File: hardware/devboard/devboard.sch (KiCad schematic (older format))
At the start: 19 parts

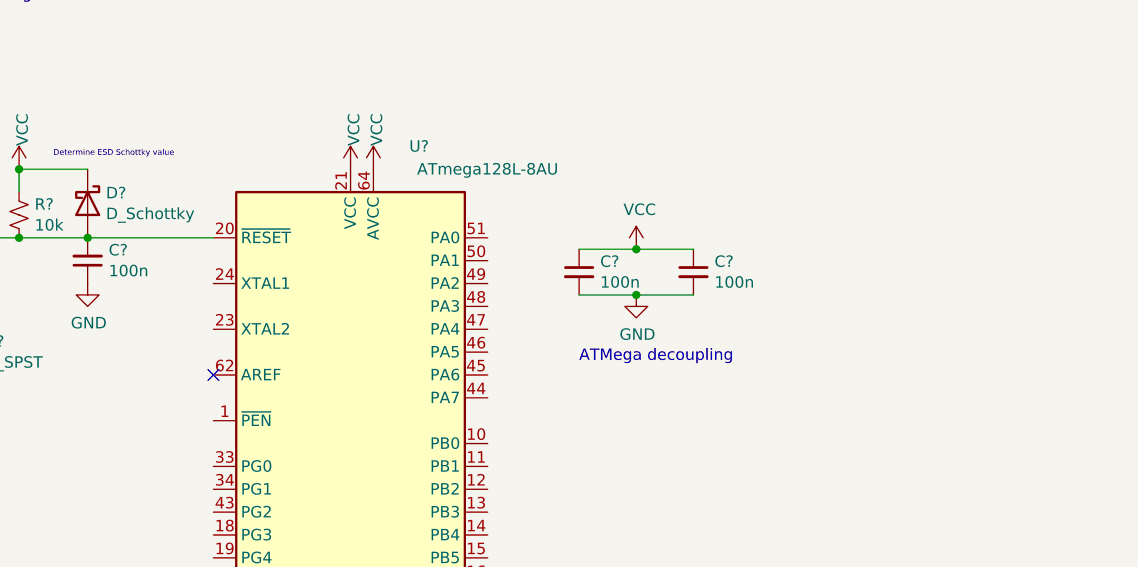
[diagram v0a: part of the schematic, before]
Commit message: Tie xtal pins to ground for now
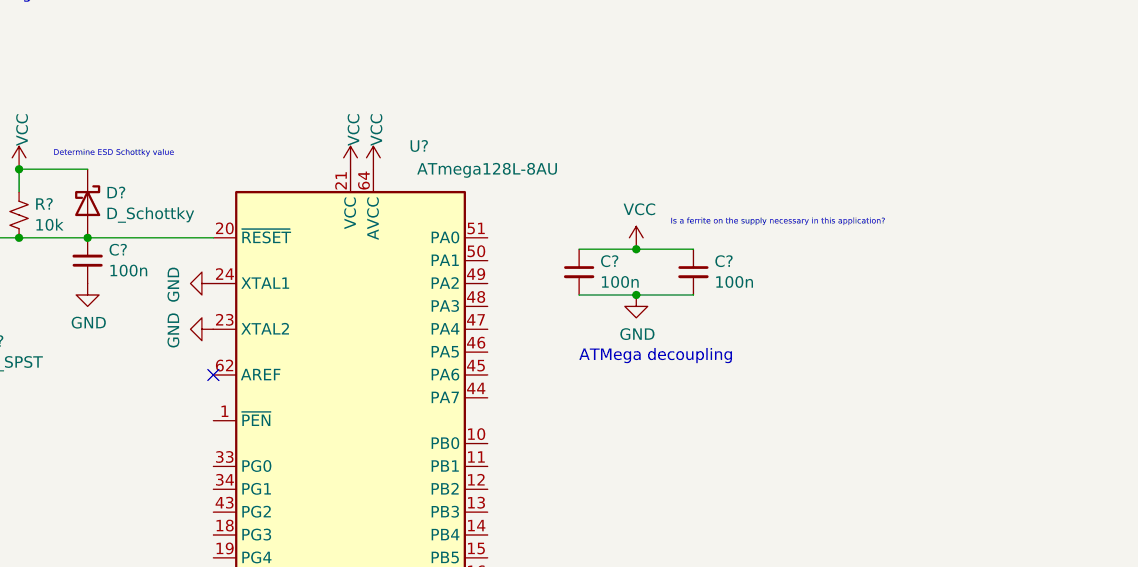
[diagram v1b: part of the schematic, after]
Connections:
- net GND: now also U?.23 (XTAL2), U?.24 (XTAL1)
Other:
- note added: "Is a ferrite on the supply necessary in this application?"
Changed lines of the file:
@@
 	1    0    0    -1
 $EndComp
+$Comp
+L power:GND #PWR?
+U 1 1 5FDE214E
+P 2050 2400
+F 0 "#PWR?" H 2050 2150 50  0001 C CNN
+F 1 "GND" H 2055 2227 50  0000 C CNN
+F 2 "" H 2050 2400 50  0001 C CNN
+F 3 "" H 2050 2400 50  0001 C CNN
+	1    2050 2400
+	0    1    1    0
+$EndComp
+$Comp
+L power:GND #PWR?
+U 1 1 5FDE278B
+P 2050 2600
+F 0 "#PWR?" H 2050 2350 50  0001 C CNN
+F 1 "GND" H 2055 2427 50  0000 C CNN
+F 2 "" H 2050 2600 50  0001 C CNN
+F 3 "" H 2050 2600 50  0001 C CNN
+	1    2050 2600
+	0    1    1    0
+$EndComp
+Text Notes 4050 2150 0    25   ~ 0
+Is a ferrite on the supply necessary in this application?
 $EndSCHEMATC

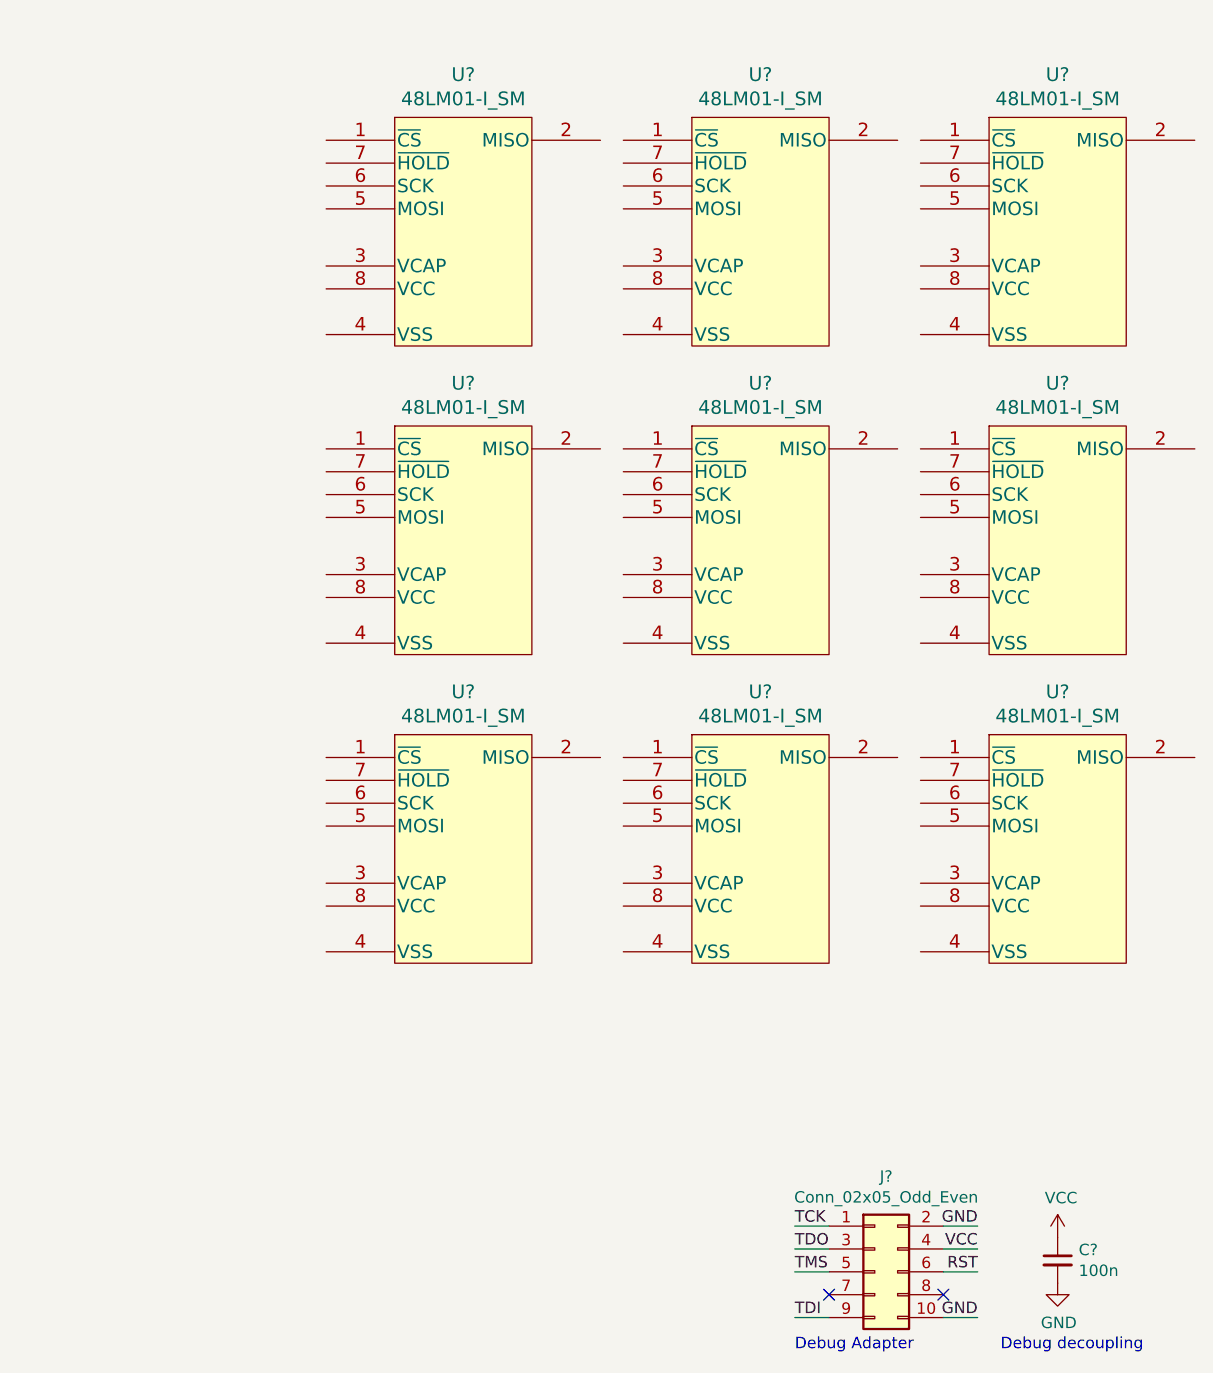
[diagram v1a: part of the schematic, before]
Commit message: Add memory banks
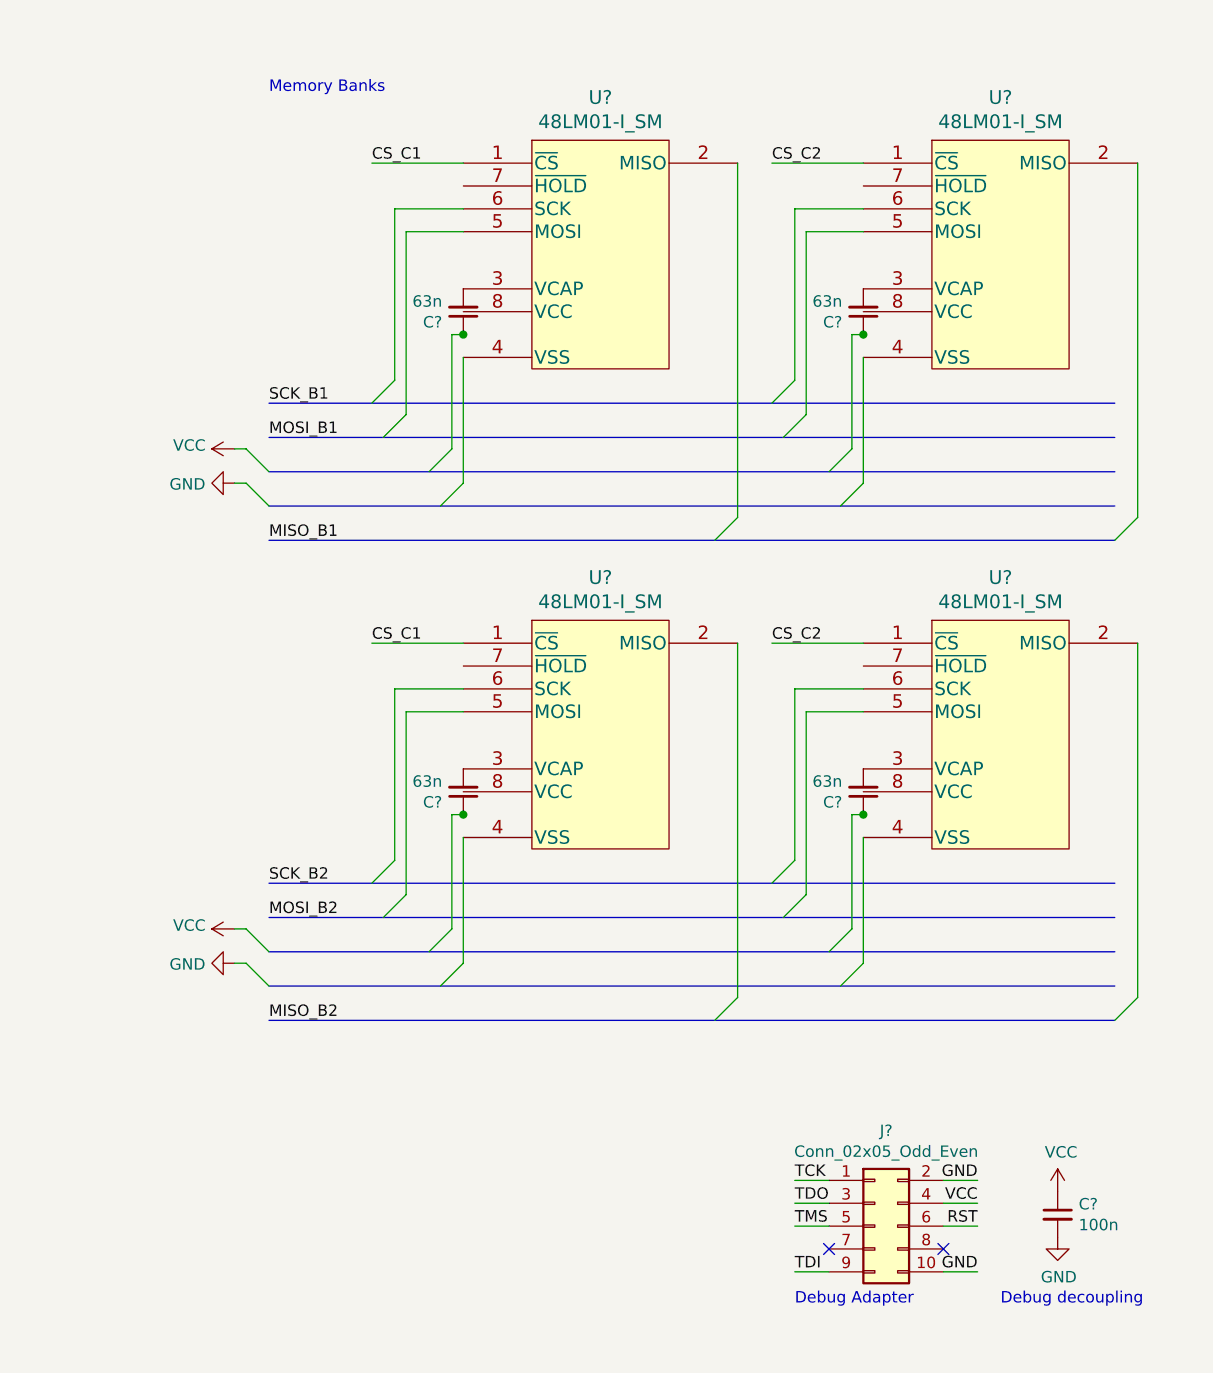
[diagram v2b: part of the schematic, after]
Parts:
- removed U? (x8): 48LM01-I_SM, SOIJ8_SM_MCH, symbol davinci:48LM01-I_SM
- added C? (x4): 63n, symbol Device:C_Small
- added U? (x3): 48LM01-I_SM, SOIJ8_SM_MCH, symbol davinci:48LM01-I_SM
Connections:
- net CS_C2: now reaches U?.1 (~CS)
- net CS_C2: now also U?.1 (~CS)
- net at U?.3 (VCAP): now also C?.2
- new net: C?.2, U?.3 (VCAP) (x3)
- new net CS_C1: U?.1 (~CS), U?.1 (~CS)
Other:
- note added: "Memory Banks"
- moved on the sheet: C?, J?, U?

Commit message: Add more memory, watchdog, buffers, test points
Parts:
- removed C? (x3): 63n, symbol Device:C_Small
- removed U? (x3): 48LM01-I_SM, SOIJ8_SM_MCH, symbol davinci:48LM01-I_SM
- added C? (x8): 63n, symbol Device:C_Small
- added C?: 100n, symbol Device:C_Small
- added R? (x3): 10k, symbol Device:R_Small_US
- added TP? (x3): TestPoint_2Pole, TestPoint:TestPoint_Bridge_Pitch2.54mm_Drill1.0mm, symbol Connector:TestPoint_2Pole
- added U? (x8): 48LM01-I_SM, SOIJ8_SM_MCH, symbol davinci:48LM01-I_SM
- added U? (x3): MC74VHCT126ADR2G, SOIC-14_NB_ONS, symbol davinci:MC74VHCT126ADR2G
- added U?: MAX6371, Package_TO_SOT_SMD:SOT-23-8, symbol Power_Supervisor:MAX6371
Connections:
- net labels added: B1_C1_HOLD, B1_C2_HOLD, B1_C3_HOLD, B1_EN, B1_MISO, B1_MOSI, B1_SCK, B2_C1_HOLD, B2_C2_HOLD, B2_C3_HOLD, B2_EN, B2_MISO, B2_MOSI, B2_SCK, B3_C1_HOLD, B3_C2_HOLD, B3_C3_HOLD, B3_EN, B3_MISO, B3_MOSI, B3_SCK, C1_CS, C2_CS, C3_CS, MISO, MOSI, SCK, WDI
- net labels removed: CS_C1, CS_C2, MISO_B1, MISO_B2, MOSI_B1, MOSI_B2, SCK_B1, SCK_B2
- wire segments 64 -> 125
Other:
- note added: "CRITICAL ELEMENTS:\nMCU\nReset circuit\nDebug circuit\nExternal tuning or clock oscillator?\nOBC connector testpads\nDedicated watchdog\nTest points"
- note added: "CRITICAL NOTES:\nCapacitors must be C0G with 60% voltage derate"
- note added: "Choose TWD, current selection is 3 seconds"
- note added: "Current limiting on set shouldn't be necessary, check this"
- note added: "Watchdog"
- note removed: "CRITICAL ELEMENTS:\nMCU\nReset circuit\nDebug circuit\nExternal tuning or clock oscillator?\nInter-element connector\nOBC connector\nDedicated watchdog\nTest points"
- note removed: "CRITICAL NOTES:\nUse Tantalum capacitors"
- note removed: "Debug decoupling"
- moved on the sheet: C?, D?, J?, R?, SW?, U?

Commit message: Add LDO for 5V supply
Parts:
- removed TP? (x3): TestPoint_2Pole, TestPoint:TestPoint_Bridge_Pitch2.54mm_Drill1.0mm, symbol Connector:TestPoint_2Pole
- added C? (x2): 1u, symbol Device:C_Small
- added TP? (x20): TestPoint, TestPoint:TestPoint_Bridge_Pitch2.54mm_Drill1.0mm, symbol Connector:TestPoint
- added U?: AP2112K-3.3, Package_TO_SOT_SMD:SOT-23-5, symbol Regulator_Linear:AP2112K-3.3
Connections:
- net labels added: +5V, ~RST
- wire segments 125 -> 148
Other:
- note added: "Test Points"
- moved on the sheet: C?, J?
